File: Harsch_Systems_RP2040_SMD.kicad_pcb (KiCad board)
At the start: 2 copper layers, 90.2 x 69.5 mm, 163 parts, among them J1 Jack-DC, J3 Conn_01x08_Female, J4 Conn_01x08_Female, J5 Conn_01x04_Female, J6 Conn_01x06_Female, J7 USB_A, Q1 BSS123, Q2 BSS123, Q3 BSS123, Q4 BSS123, Q5 BCP56, Q6 BCP56, Q7 BCP56, Q8 BCP56, SW1 SW_MEC_5E, U1 XC6210B332MR, U10 TLV9304IDR, U11 TPS56339DDC, U3 RP2040, U4 W25Q32JVSSIQ_TR, U5 TLV9004xRUCR, U6 ELQ3H7, U7 TLV9004xRUCR, U8 ELQ3H7, U9 ELQ3H7, Y1 12MHz

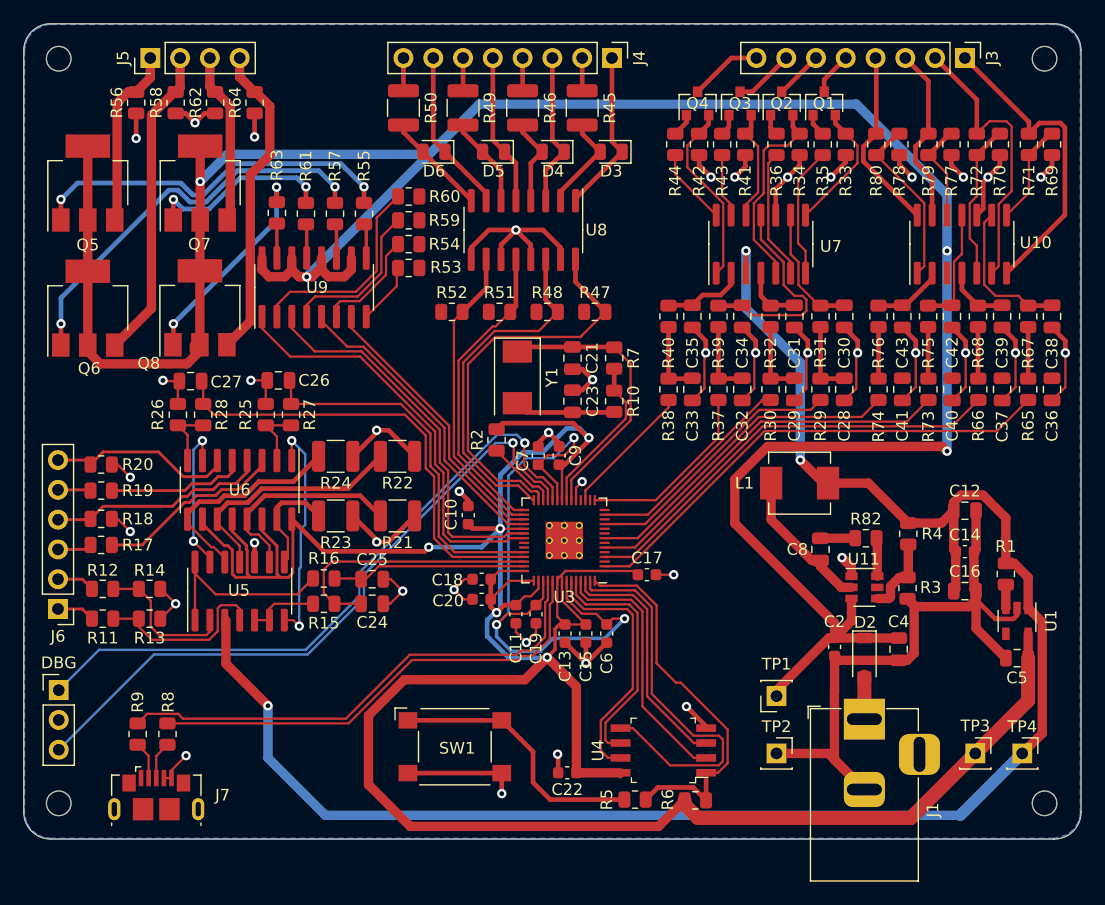
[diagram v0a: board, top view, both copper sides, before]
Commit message: Adjusted some tracks and vias for better heat dissipation
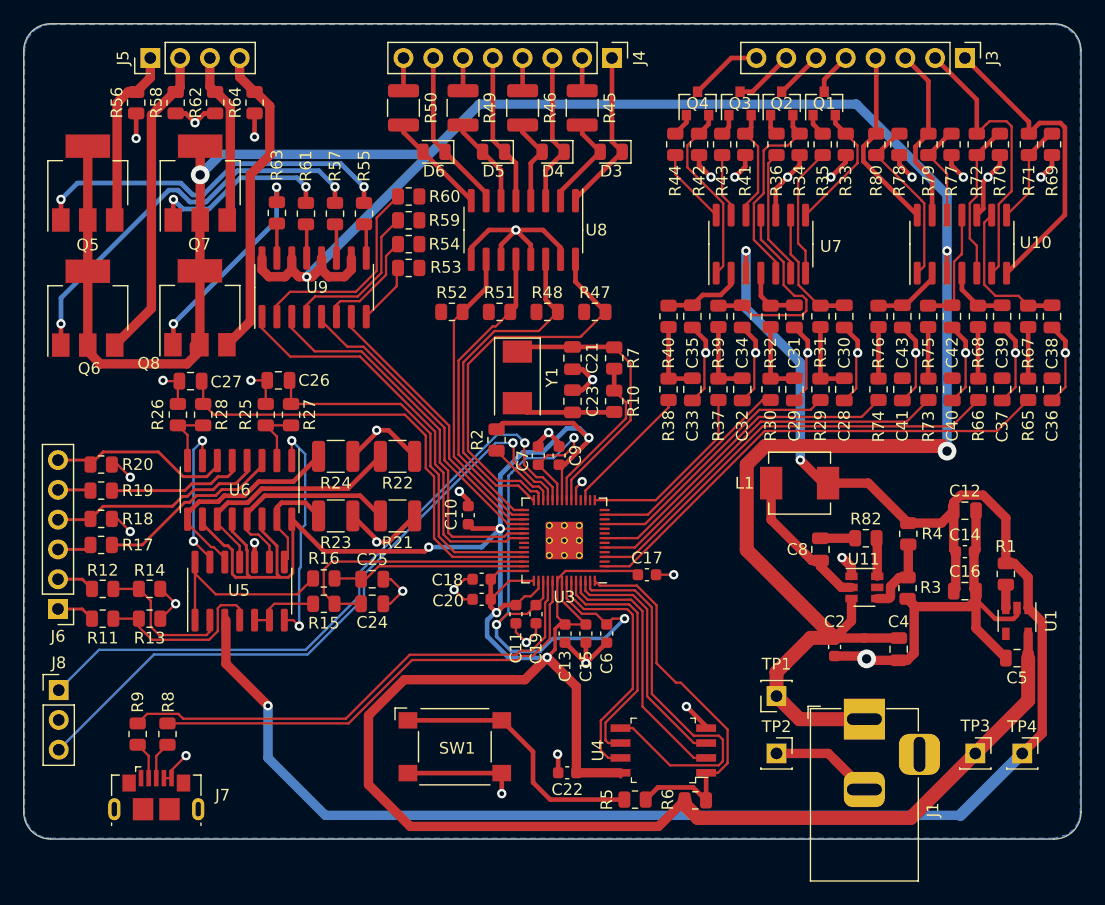
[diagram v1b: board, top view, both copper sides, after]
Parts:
- removed D2: D_Schottky, Diode_SMD:D_SOD-123
- removed REF** (x4): MountingHole_2.1mm, MountingHole:MountingHole_2.1mm
- renumbered DBG to J8
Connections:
- J1 pad 1: Net-(D2-Pad2) -> +24V
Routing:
- net +24V: track 219.0 -> 229.7 mm
- net GND: track 248.4 -> 239.5 mm, vias 42 -> 43
- net Net-(D2-Pad2): track 3.62 -> 0.00 mm

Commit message: Added an I2C QWIIC Connector
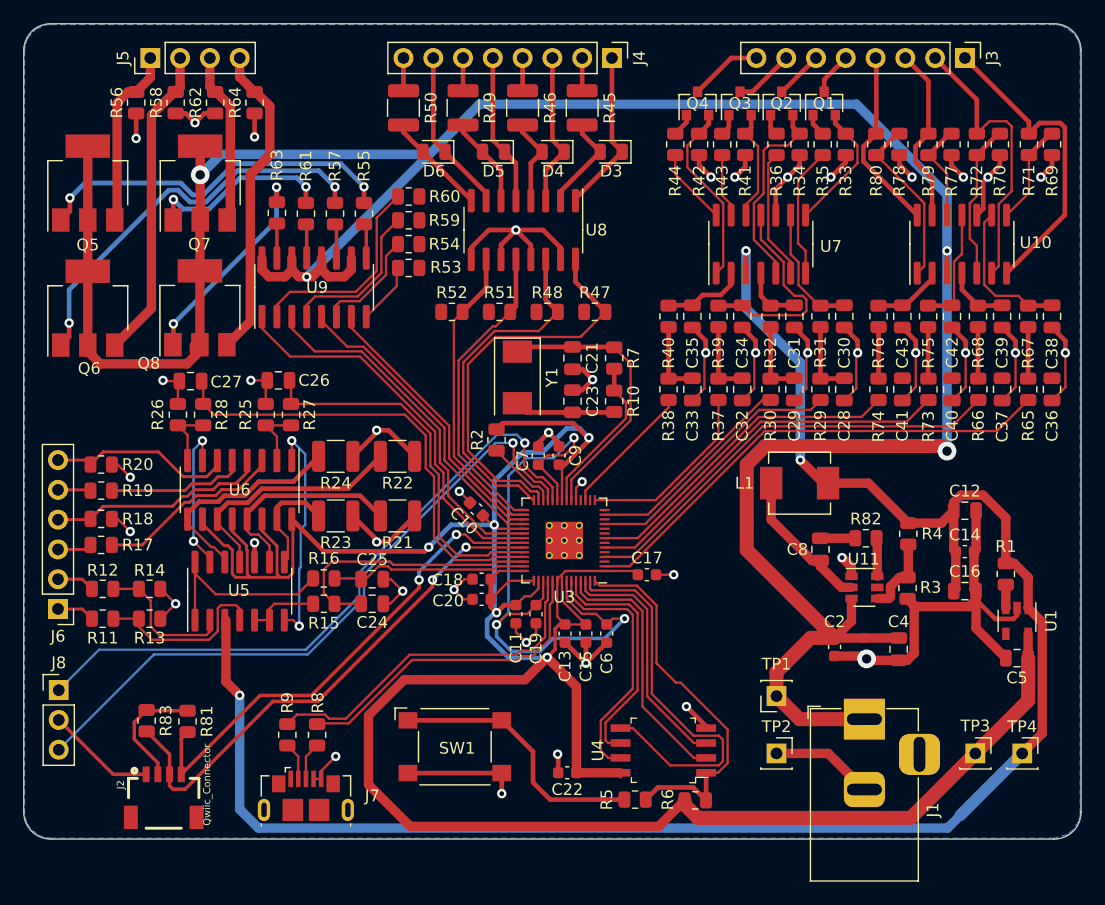
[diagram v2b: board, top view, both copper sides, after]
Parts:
- added J2: Qwiic_Connector, Connectors:1X04_1MM_RA, F.Cu at (102.4, 118.4)
- added R81: 2.2k, Resistor_SMD:R_0805_2012Metric, F.Cu at (104.5, 113.9)
- added R83: 2.2k, Resistor_SMD:R_0805_2012Metric, F.Cu at (101.0, 113.9)
- moved J7 12.8 mm to (114.6, 120.3)
- moved R8 12.8 mm to (115.5, 115.1)
- moved R9 12.8 mm to (113.0, 115.1)
- moved C10 0.86 mm to (129.1, 95.8), turned to 135 degrees
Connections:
- U3 pad 36: Net-(U3-Pad36) -> /SCL
- U3 pad 37: Net-(U3-Pad37) -> /SDA
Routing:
- net /SDA: track 0.00 -> 44.7 mm, vias 0 -> 2
- net /SCL: track 0.00 -> 42.6 mm, vias 0 -> 2
- net /USB_D-: track 43.0 -> 30.3 mm
- net /USB_D+: track 40.7 -> 27.9 mm
- net Net-(J2-Pad2): track 0.00 -> 10.3 mm
- net GND: track 239.5 -> 248.7 mm
- net +5V: track 154.9 -> 159.8 mm
- net /GPIO22: track 33.0 -> 30.9 mm
- net /GPIO23: track 35.7 -> 33.7 mm
